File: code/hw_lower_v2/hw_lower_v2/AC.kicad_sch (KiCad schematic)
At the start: 32 parts, among them K1 HE-S 2, Q1 BSS138, Q2 BSS138, Q3 BSS138, T1 Transformer_1P_1S, U1 BRCS02C, U2 BL0942

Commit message: further lower board sch work
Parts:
- added C10, C9: 22uF 25V, Capacitor_SMD:C_1210_3225Metric, symbol Device:C
- added C11: 100n, Capacitor_SMD:C_0805_2012Metric, symbol Device:C
- added R33: 20K, Resistor_SMD:R_0603_1608Metric, symbol Device:R
- C1, C2, C3, C7, C8: footprint (none) -> Capacitor_SMD:C_0805_2012Metric
- R1, R2, R3, R4: footprint (none) -> Resistor_SMD:R_1206_3216Metric
- R10, R13, R14, R15, R16: value 20K -> 10K; footprint (none) -> Resistor_SMD:R_0603_1608Metric
- R11, R12, R17, R31, R5, R6, R7, R8, R9: footprint (none) -> Resistor_SMD:R_0603_1608Metric
- R32: value 100K -> 10K; footprint (none) -> Resistor_SMD:R_0603_1608Metric
- U2: footprint (none) -> Package_SO:SSOP-10-1EP_3.9x4.9mm_P1mm_EP2.1x3.3mm
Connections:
- net +12V: now also C10.1, C11.1, C9.1
- net AC_RELAY_PWM: now also R33.2
- net Earth_Protective: now also C10.2, C11.2, C9.2, R33.1
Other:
- moved on the sheet: C1, C2, R31, R32

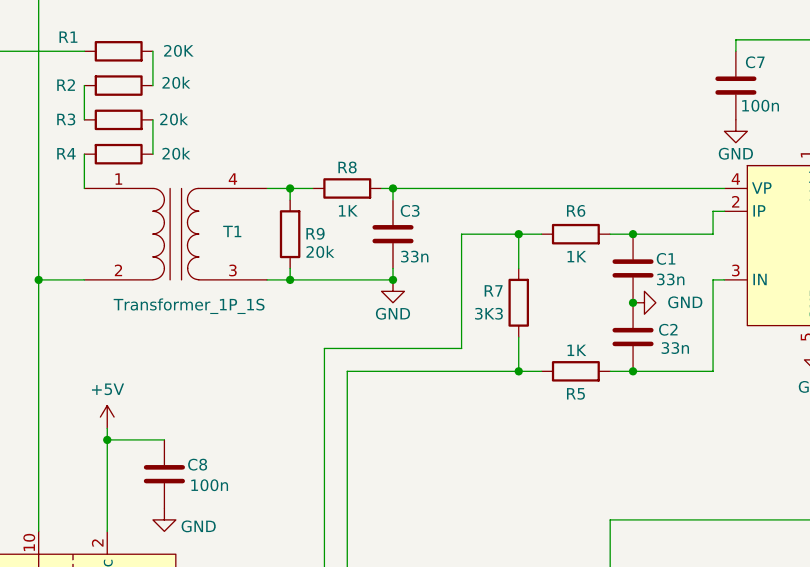
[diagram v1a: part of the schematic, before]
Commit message: add 12V voltage inverter and polish
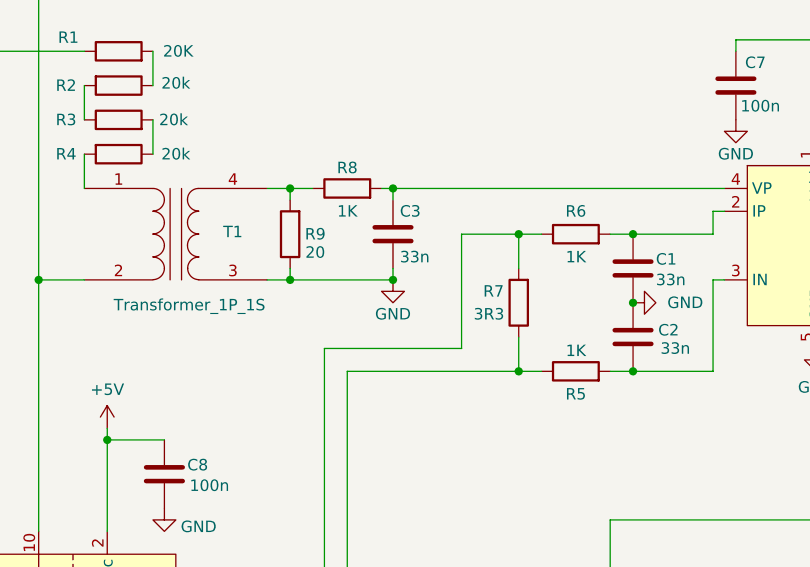
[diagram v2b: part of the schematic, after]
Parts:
- R7: value 3K3 -> 3R3
- R9: value 20k -> 20
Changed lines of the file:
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@@
 			)
 		)
-		(property "Value" "20k"
-			(at 97.282 56.642 0)
+		(property "Value" "20"
+			(at 96.774 56.642 0)
 			(effects
 				(font
@@
 			)
 		)
-		(property "Value" "3K3"
+		(property "Value" "3R3"
 			(at 116.078 63.5 0)
 			(effects

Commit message: schematic is done
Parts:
- removed C10, C9: 22uF 25V, Capacitor_SMD:C_1210_3225Metric, symbol Device:C
- added C22: 10u, symbol Device:C_Polarized
- added R42: 20K 1%, Resistor_SMD:R_1206_3216Metric, symbol Device:R
- added R43: TBD, Resistor_SMD:R_0603_1608Metric, symbol Device:R
- R1: value 20K -> 20K 1%
- R11: value 20k -> 5k6
- R12: value 20k -> 10k
- R2, R3, R4: value 20k -> 20K 1%
- R33: value 20K -> TBD
- R7: value 3R3 -> 1R6 0.1%
- R9: value 20 -> 24R 0.1%
- T1: value Transformer_1P_1S -> TS3193-2C 2mA/2mA; JLCPCB Part # (none) -> C2896606
- U2: JLCPCB Part # (none) -> C2837510
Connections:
- net +12V: now also C22.1
- net AC_RELAY_PWM: now also R43.1; no longer Q3.1 (G), R33.2
- net Earth_Protective: now also C22.2
- net N_in: now also R4.1; no longer R1.1
- net at R3.2: now also R2.2; no longer R4.1
- net at R4.2: now also R3.1; no longer T1.1 (AA)
- new net: Q3.1 (G), R33.2, R43.2
- new net: R42.1, T1.1 (AA)
- new net: R1.1, R42.2
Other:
- moved on the sheet: C1, C11, C2, C3, C7, R17, R31, R32, R5, R6, R7, R8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

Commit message: finishing up sch and creating footprints
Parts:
- K1: footprint (none) -> multi_new:panasonic HE-s
- U1: footprint (none) -> multi_new:BRCS02C
- renumbered C8 to C1, C22 to C2, C11 to C4, C1 to C5, C2 to C6, Q3 to Q1, Q1 to Q3, R1 to R10, R42 to R11, R10 to R12, R9 to R13, R8 to R14, R33 to R15, R7 to R16, R43 to R17, R6 to R18, R5 to R19, R15 to R20, R13 to R21, R16 to R22, R14 to R23, R11 to R24, R17 to R25, R12 to R26, R32 to R27, R31 to R28, R3 to R7, R4 to R8, R2 to R9
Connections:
- net +12V: now also K1.2; no longer K1.5
- net AC_RELAY_SENSE: now also K1.4; no longer K1.6
- net Earth_Protective: now also K1.3; no longer K1.7
- net L_out: now also K1.5; no longer K1.10
- net N_out: now also K1.7; no longer K1.12
- net at D1.2 (A), Q1.3 (D): now also K1.1; no longer K1.8
- net at U1.9: now also K1.8; no longer K1.1
- net at U1.11: now also K1.6; no longer K1.3

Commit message: wip
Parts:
- R10, R11, R7, R8, R9: value 20K 1% -> 20K
- T1: JLCPCB Part # C2896606 -> (none); LCSC (none) -> C2896606
- U2: JLCPCB Part # C2837510 -> (none); LCSC (none) -> C2837510

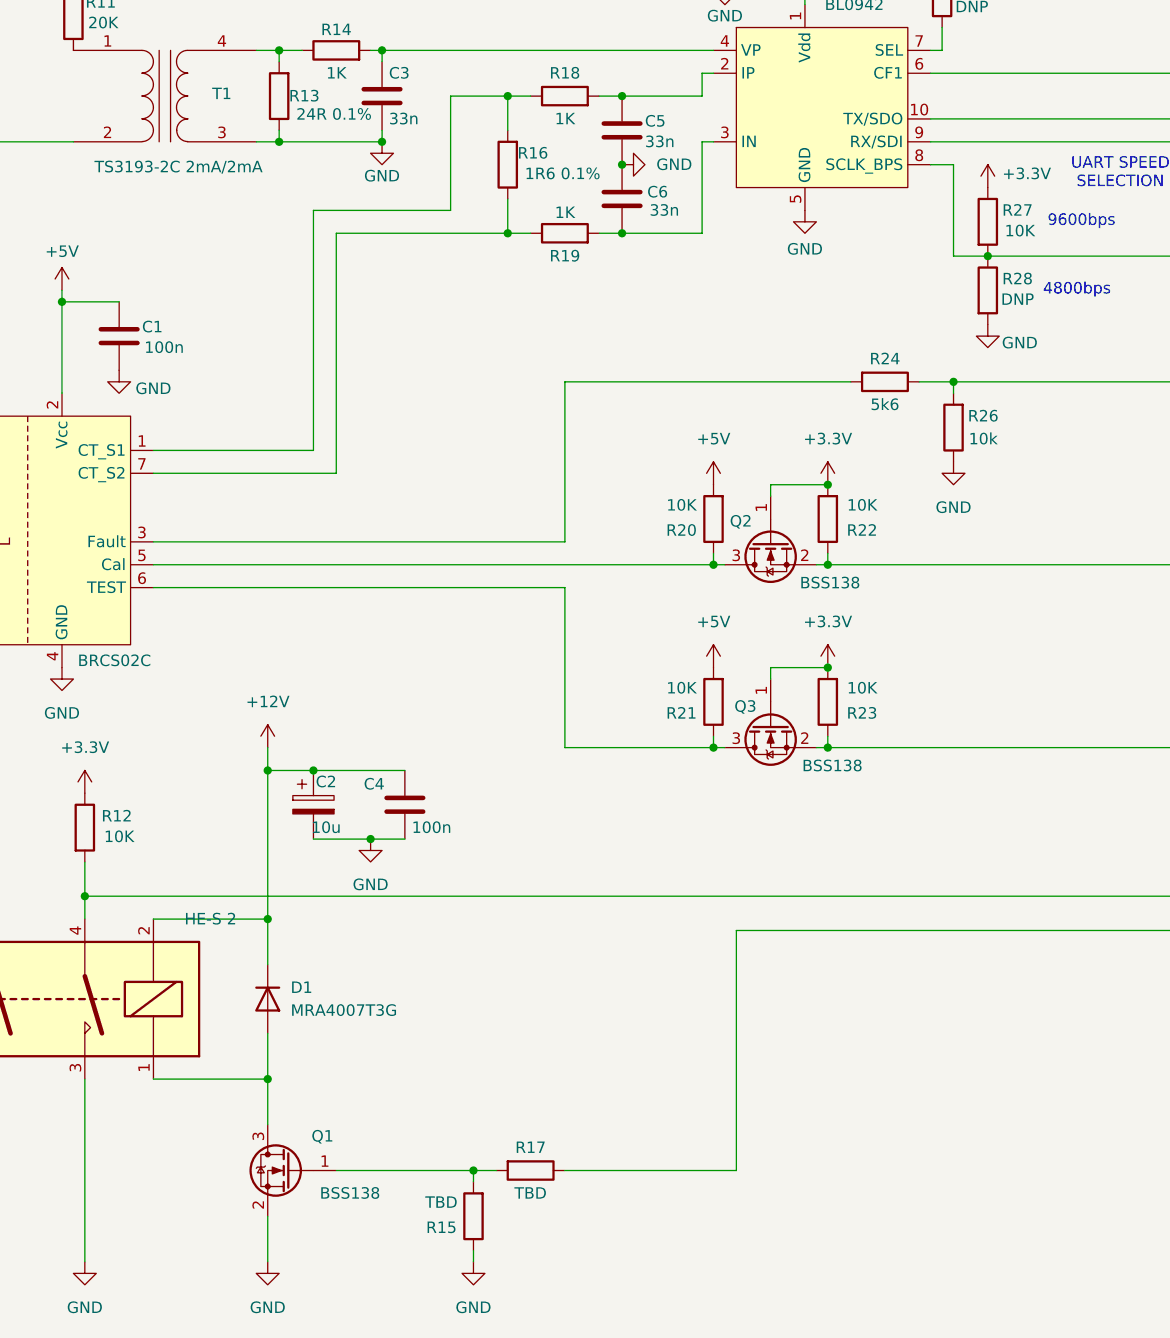
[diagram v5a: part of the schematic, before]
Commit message: finished schematic, started first pass of layout
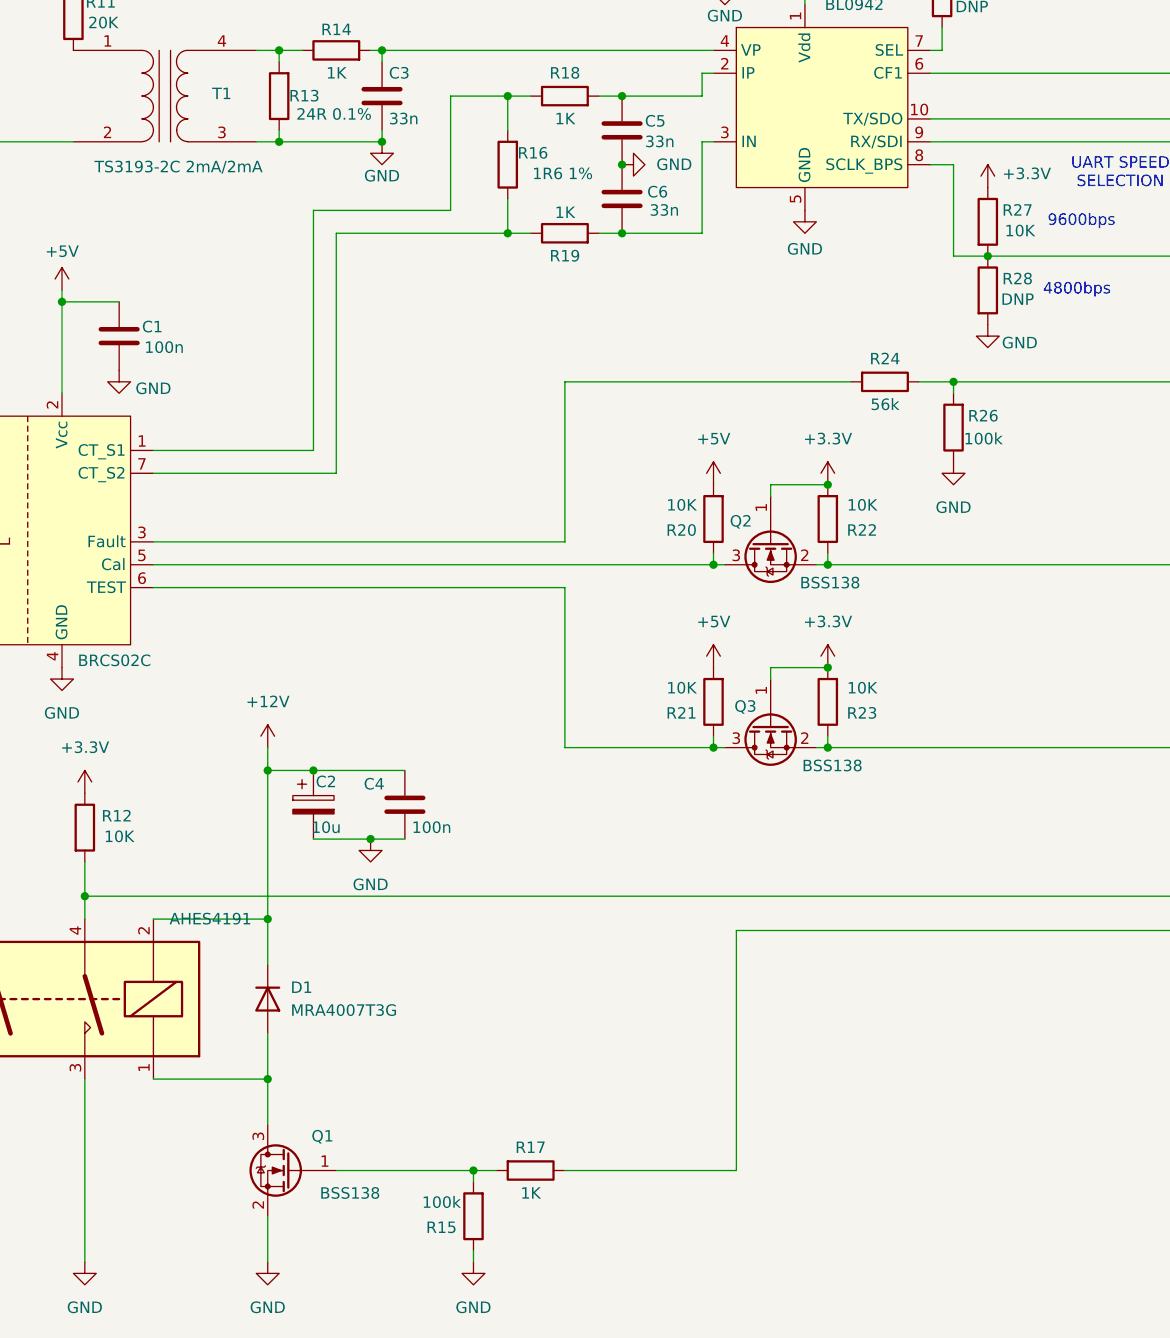
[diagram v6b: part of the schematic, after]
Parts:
- C1, C4, C7: LCSC (none) -> C38141
- C2: value 10u -> 10u; footprint (none) -> Capacitor_SMD:CP_Elec_4x5.4; LCSC (none) -> C72485
- C3, C5, C6: footprint Capacitor_SMD:C_0805_2012Metric -> Capacitor_SMD:C_0603_1608Metric; LCSC (none) -> C327162
- D1: LCSC (none) -> C47921
- K1: value HE-S 2 -> AHES4191; LCSC (none) -> C719192
- Q1, Q2, Q3: LCSC (none) -> C112239
- R10, R11, R7, R8, R9: LCSC (none) -> C706407
- R12, R20, R21, R22, R23, R27: LCSC (none) -> C25804
- R13: LCSC (none) -> C317933
- R14, R18, R19: LCSC (none) -> C21190
- R15: value TBD -> 100k; LCSC (none) -> C25804
- R16: value 1R6 0.1% -> 1R6 1%; LCSC (none) -> C365113
- R17: value TBD -> 1K; LCSC (none) -> C21190
- R24: value 5k6 -> 56k; LCSC (none) -> C5250755
- R26: value 10k -> 100k; LCSC (none) -> C25804
- T1: footprint (none) -> multi_new:TS3193-2C
- U1: footprint multi_new:BRCS02C -> multi_new:BRCS02C_1
- U2: footprint Package_SO:SSOP-10-1EP_3.9x4.9mm_P1mm_EP2.1x3.3mm -> JLCPCB:SSOP-10_L4.9-W3.9-P1.00-LS6.0-BL

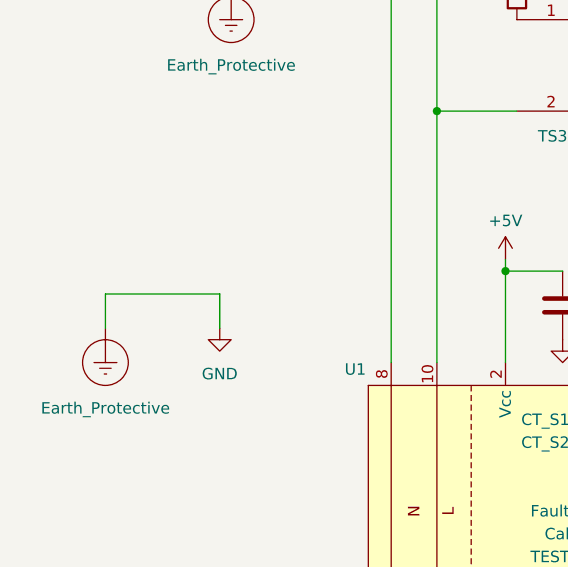
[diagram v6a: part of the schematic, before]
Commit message: Preliminary pcb component placement done
PCB size currently is around 100mm X 100mm with the mezanine board being ~40mm x 100mm
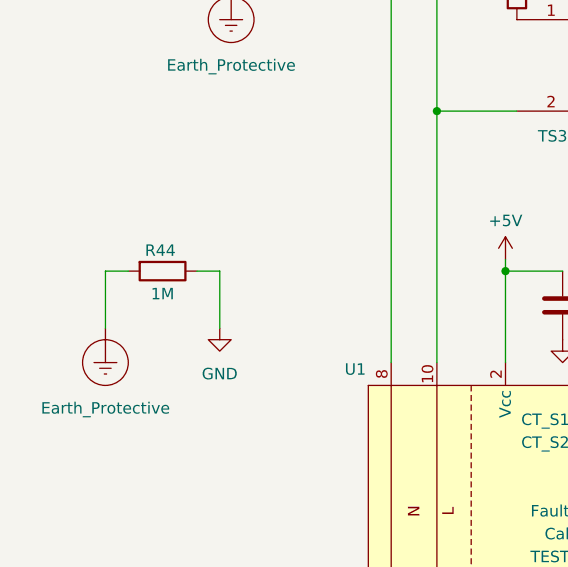
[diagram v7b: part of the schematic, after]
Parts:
- added R44: 1M, Resistor_SMD:R_1206_3216Metric, symbol Device:R
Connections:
- net Earth_Protective: now also R44.2; no longer C1.2, C2.2, C3.2, C4.2, C5.2, C6.1, C7.2, K1.3, Q1.2 (S), R13.1, R15.1, R26.1, R28.2, T1.3 (SA), U1.4 (GND), U2.5 (GND)
- new net GND: C1.2, C2.2, C3.2, C4.2, C5.2, C6.1, C7.2, K1.3, Q1.2 (S), R13.1, R15.1, R26.1, R28.2, R44.1, T1.3 (SA), U1.4 (GND), U2.5 (GND)
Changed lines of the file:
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@@
 	(wire
 		(pts
+			(xy 39.37 77.47) (xy 41.91 77.47)
+		)
+		(stroke
+			(width 0)
+			(type default)
+		)
+	)
+	(wire
+		(pts
 			(xy 170.18 62.23) (xy 172.72 62.23)
 		)
@@
 	(wire
 		(pts
-			(xy 29.21 83.82) (xy 29.21 80.01)
-		)
-		(stroke
-			(width 0)
-			(type default)
-		)
-	)
-	(wire
-		(pts
 			(xy 109.22 58.42) (xy 109.22 59.69)
 		)
@@
 	(wire
 		(pts
+			(xy 29.21 77.47) (xy 31.75 77.47)
+		)
+		(stroke
+			(width 0)
+			(type default)
+		)
+	)
+	(wire
+		(pts
 			(xy 69.85 26.67) (xy 74.93 26.67)
 		)
@@
 	(wire
 		(pts
+			(xy 29.21 77.47) (xy 29.21 83.82)
+		)
+		(stroke
+			(width 0)
+			(type default)
+		)
+	)
+	(wire
+		(pts
 			(xy 116.84 67.31) (xy 101.6 67.31)
 		)
@@
 	(wire
 		(pts
-			(xy 144.78 69.85) (xy 135.89 69.85)
+			(xy 41.91 77.47) (xy 41.91 83.82)
 		)
 		(stroke
@@
 	(wire
 		(pts
-			(xy 43.18 41.91) (xy 43.18 45.72)
+			(xy 144.78 69.85) (xy 135.89 69.85)
 		)
 		(stroke
@@
 	(wire
 		(pts
-			(xy 41.91 80.01) (xy 41.91 83.82)
+			(xy 43.18 41.91) (xy 43.18 45.72)
 		)
 		(stroke
@@
 	(wire
 		(pts
-			(xy 29.21 80.01) (xy 41.91 80.01)
-		)
-		(stroke
-			(width 0)
-			(type default)
-		)
-	)
-	(wire
-		(pts
 			(xy 96.52 163.83) (xy 96.52 158.75)
 		)
@@
 					(unit 1)
 				)
+			)
+		)
+	)
+	(symbol
+		(lib_id "Device:R")
+		(at 35.56 77.47 270)
+		(unit 1)
+		(exclude_from_sim no)
+		(in_bom yes)
+		(on_board yes)
+		(dnp no)
+		(property "Reference" "R44"
+			(at 35.306 75.184 90)
+			(effects
+				(font
+					(size 1.27 1.27)
+				)
+			)
+		)
+		(property "Value" "1M"
+			(at 35.56 80.01 90)
+			(effects
+				(font
+					(size 1.27 1.27)
+				)
+			)
+		)
+		(property "Footprint" "Resistor_SMD:R_1206_3216Metric"
+			(at 35.56 75.692 90)
+			(effects
+				(font
+					(size 1.27 1.27)
+				)
+				(hide yes)
+			)
+		)
+		(property "Datasheet" "~"
+			(at 35.56 77.47 0)
+			(effects
+				(font
+					(size 1.27 1.27)
+				)
+				(hide yes)
+			)
+		)
+		(property "Description" "Resistor"
+			(at 35.56 77.47 0)
+			(effects
+				(font
+					(size 1.27 1.27)
+				)
+				(hide yes)
+			)
+		)
+		(property "LCSC" "C25804"
+			(at 35.56 77.47 0)
+			(effects
+				(font
+					(size 1.27 1.27)
+				)
+				(hide yes)
+			)
+		)
+		(pin "1"
+		)
+		(pin "2"
+		)
+		(instances
+			(project "hw_lower_v2"
+				(path "/c5175f1c-553a-46da-abbd-483c59ad8dfa/f685e69a-3cdf-4f53-94e9-452320868ecf"
+					(reference "R44")
+					(unit 1)
+				)
